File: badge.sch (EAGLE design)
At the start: 142 parts, among them CN4 MicroUSB, IC3 MEGA8-AI, T1 MMUN2133LT1G, U1 TPS61090RSAR, U2 MCP73871, Y1 16.00MHz

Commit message: Cut down the LEDs to 50 and added filter caps for each
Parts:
- removed +5V, GND, MISO, MOSI, RST, SCK: TPTP17R, testpad:TPTP17R
- removed LED100, LED51, LED52, LED53, LED54, LED55, LED56, LED57, LED58, LED59, LED60, LED61, LED62, LED63, LED64, LED65, LED66, LED67, LED68, LED69, LED70, LED71, LED72, LED73, LED74, LED75, LED76, LED77, LED78, LED79, LED80, LED81, LED82, LED83, LED84, LED85, LED86, LED87, LED88, LED89, LED90, LED91, LED92, LED93, LED94, LED95, LED96, LED97, LED98, LED99: WS2812B5050-NARROW, defcon:WS2812B5050-NARROW
- added C10, C11, C12, C13, C14, C15, C16, C17, C18, C19, C20, C21, C22, C23, C24, C25, C26, C27, C28, C29, C30, C31, C32, C33, C34, C35, C36, C37, C38, C39, C40, C41, C42, C43, C44, C45, C46, C47, C48, C49, C50, C51, C52, C53, C54, C55, C56, C57, C58, C9: (no value), resistor:C-USC0603
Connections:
- removed net HR_SET: JP1.1, MISO.TP
- removed net MIN_SET: JP1.3, SCK.TP
- new net MISO: IC3.PB4(MISO), JP1.1
- new net N$17: C9.1, LED1.VDD
- new net N$18: C9.2, LED1.GND
- new net SCK: IC3.PB5(SCK), JP1.3
- net +5V: no longer +5V.TP
- net GND: no longer GND.TP
- net MOSI: now also IC3.PB3(MOSI/OC2); no longer MOSI.TP
- net RESET_PROG: no longer RST.TP

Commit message: Added accelerometer circuitry
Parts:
- added C59: 0.1uF, resistor:C-USC0805
- added C60, C61: 10µF, resistor:C-USC0805
- added D2: 1N4148, led:LEDCHIP-LED0805
- added JP2: (no value), microbuilder:HEADER-1X870MIL
- added JP3: (no value), microbuilder:HEADER-1X3ROUND
- added Q1, Q2: BSS138, microbuilder:MOSFET-NWIDE
- added R10, R11, R12, R15, R18, R9: 10K, resistor:R-US_M0805
- added U3: LIS3DHTR, microbuilder:ACCEL_LIS3DHTR
- added U4: MIC5225-3.3, microbuilder:VREG_SOT23-5
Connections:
- new net 3.3V: C59.1, C60.1, JP2.2, Q1.G, Q2.G, R10.2, R11.2, R9.2, U3.VDD, U3.VDDIO, U4.OUT
- new net ADC1: JP3.1, U3.ADC1
- new net ADC2: JP3.2, U3.ADC2
- new net ADC3: JP3.3, U3.ADC3
- new net CS: D2.C, JP2.7
- new net INT1: JP2.8, U3.INT1
- new net N$19: D2.A, R9.1, U3.CS
- new net SCL: JP2.4, Q2.D, R15.1
- new net SCL_3.3V: Q2.S, R11.1, U3.SCL
- new net SDA: JP2.5, Q1.D, R12.1
- new net SDA_3.3V: Q1.S, R10.1, U3.SDA
- new net SDO: JP2.6, R18.2, U3.SDO
- new net VIN: C61.1, JP2.1, R12.2, R15.2, U4.EN, U4.IN
- net GND: now also C59.2, C60.2, C61.2, JP2.3, R18.1, U3.GND@1, U3.GND@2, U3.RES(GND), U4.GND
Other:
- note added: "* CS needs to be set off board to select SPI or I2C"
- note added: "Bus Selection"
- note added: "CS High = I2C, Low = SPI"
- note added: "Defaults to I2C as-is (R8)"
- note added: "I2C"
- note added: "LED Array"
- note added: "MCU Circuitry"
- note added: "Power Circuitry"
- note added: "SCL (Pin 4) = Serial Clock"
- note added: "SD0 (Pin 7) = SA0/Address LSB"
- note added: "SDA (Pin 6) = Data In (MOSI)"
- note added: "SDA (Pin 6) = Serial Data"
- note added: "SDO (Pin 7) = Data Out (MISO)"
- note added: "SDO pulled low by default (R1) to set I2C address LSB to 0"
- note added: "SPI"
- note added: "Set SJ1 to make I2C"
- note added: "address LSB 1"
- moved on the sheet: BT1, C1, C2, C4, C6, C7, C8, CHRG/LBO, CN4, DONE, JP1, L1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

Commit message: Added switches, status lights, RX/TX Headers
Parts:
- removed D2: 1N4148, led:LEDCHIP-LED0805
- removed JP3: (no value), microbuilder:HEADER-1X3ROUND
- added C62: 1F, resistor:CPOL-USE5-8.5
- added C63, C64, C65, C66, C67, C68: 100nF, resistor:C-USC0805
- added R19: 470, resistor:R-US_R0805
- added R21, R22, R23: 220, resistor:R-US_M0805
- added R24, R25, R26, R27, R28, R29: 1k, resistor:R-US_M0805
- added S1: (no value), adafruit:EG1218S
- added STAT1, STAT2, STAT3: GREEN, piboy_new:ADAFRUIT_LEDCHIPLED_0603
- added SV1: (no value), con-lstb:MA04-2
- added SW1, SW2, SW3, SW4, SW5, SW6: (no value), adafruit:SWITCH_PUSHBUTTONEVQ-PE
- JP1: device pinhead+:PINHD-2X3SMT -> pinhead:PINHD-2X4
- JP2: device microbuilder:HEADER-1X870MIL -> pinhead:PINHD-1X2
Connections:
- removed net CS: D2.C, JP2.7
- removed net ENABLE: R13.2, U1.EN
- new net BOOST_ENABLE: R13.2, S1.P, U1.EN
- new net CE\: SV1.6
- new net CSN: SV1.5
- new net N$20: R21.2, STAT2.C
- new net N$21: R22.2, STAT3.C
- new net N$22: R23.2, STAT1.C
- new net N$23: R24.2, SW1.P$2
- new net N$30: R26.2, SW3.P$2
- new net N$31: R28.2, SW5.P$2
- new net N$32: R29.2, SW6.P$2
- new net N$33: R27.2, SW4.P$2
- new net N$34: R25.2, SW2.P$2
- new net NEO-DOUT: IC3.PD6(AIN0), R19.1
- new net PIEZO: IC3.PB1(OC1A), JP2.1
- new net RX: IC3.PD0(RXD), JP1.7
- new net STAT1: IC3.PD2(INT0), STAT1.A
- new net STAT2: IC3.PD3(INT1)
- new net STAT3: IC3.PD4(XCK/T0), STAT3.A
- new net STAT4: STAT2.A
- new net SW1: C63.1, IC3.PC0(ADC0), R24.1
- new net SW2: C64.1, IC3.PC1(ADC1), R25.1
- new net SW3: C65.1, IC3.PC2(ADC2), R26.1
- new net SW4: C66.1, IC3.PC3(ADC3), R27.1
- new net SW5: C67.1, IC3.ADC6, R28.1
- new net SW6: C68.1, IC3.ADC7, R29.1
- new net TX: IC3.PD1(TXD), JP1.8
- net +5V: now also C62.+
- net 3.3V: now also R9.1, SV1.7; no longer JP2.2, R9.2
- net ADC1: no longer JP3.1
- net ADC2: no longer JP3.2
- net ADC3: no longer JP3.3
- net GND: now also C62.-, JP2.2, R21.1, R22.1, R23.1, S1.S, SV1.8, SW1.P$1, SW2.P$1, SW3.P$1, SW4.P$1, SW5.P$1, SW6.P$1; no longer JP2.3
- net INT1: no longer JP2.8
- net MISO: now also SV1.2
- net MOSI: now also SV1.3
- net N$19: now also R9.2; no longer D2.A, R9.1
- net SCK: now also SV1.4
- net SCL: now also IC3.PC5(ADC5/SCL); no longer JP2.4
- net SDA: now also IC3.PC4(ADC4/SDA); no longer JP2.5
- net SDO: no longer JP2.6
- net VIN: no longer JP2.1
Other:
- moved on the sheet: C59, C60, C61, Q1, Q2, R10, R11, R12, R15, R18, R9, U3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

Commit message: -wired all the pixels -cleaned up the schematic
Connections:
- removed net N$18: C9.2, LED1.GND
- new net N$24: LED1.DO, LED2.DI
- new net N$25: LED3.DO, LED4.DI
- new net N$26: LED4.DO, LED5.DI
- new net N$27: LED5.DO, LED6.DI
- new net N$37: LED6.DO, LED7.DI
- new net N$38: LED7.DO, LED8.DI
- new net N$39: LED8.DO, LED9.DI
- new net N$40: LED10.DI, LED9.DO
- new net N$41: LED10.DO, LED11.DI
- new net N$42: LED11.DO, LED12.DI
- new net N$43: LED12.DO, LED13.DI
- new net N$44: LED13.DO, LED14.DI
- new net N$45: LED14.DO, LED15.DI
- new net N$46: LED15.DO, LED16.DI
- new net N$47: LED16.DO, LED17.DI
- new net N$48: LED17.DO, LED18.DI
- new net N$49: LED18.DO, LED19.DI
- new net N$50: LED19.DO, LED20.DI
- new net N$51: LED20.DO, LED21.DI
- new net N$52: LED21.DO, LED22.DI
- new net N$53: LED22.DO, LED23.DI
- new net N$54: LED23.DO, LED24.DI
- new net N$55: LED24.DO, LED25.DI
- new net N$56: LED25.DO, LED26.DI
- new net N$57: LED26.DO, LED27.DI
- new net N$58: LED27.DO, LED28.DI
- new net N$59: LED28.DO, LED29.DI
- new net N$60: LED29.DO, LED30.DI
- new net N$61: LED30.DO, LED31.DI
- new net N$62: LED31.DO, LED32.DI
- new net N$63: LED32.DO, LED33.DI
- new net N$64: LED33.DO, LED34.DI
- new net N$65: LED34.DO, LED35.DI
- new net N$66: LED35.DO, LED36.DI
- new net N$67: LED36.DO, LED37.DI
- new net N$68: LED37.DO, LED38.DI
- new net N$69: LED38.DO, LED39.DI
- new net N$70: LED39.DO, LED40.DI
- new net N$71: LED40.DO, LED41.DI
- new net N$72: LED41.DO, LED42.DI
- new net N$73: LED42.DO, LED43.DI
- new net N$74: LED43.DO, LED44.DI
- new net N$75: LED44.DO, LED45.DI
- new net N$76: LED45.DO, LED46.DI
- new net N$77: LED46.DO, LED47.DI
- new net N$78: LED47.DO, LED48.DI
- new net N$79: LED48.DO, LED49.DI
- new net N$80: LED49.DO, LED50.DI
- new net PIXEL_DATA: LED1.DI, R19.2
- net +5V: now also C10.1, C11.1, C12.1, C13.1, C14.1, C15.1, C16.1, C17.1, C18.1, C19.1, C20.1, C21.1, C22.1, C23.1, C24.1, C25.1, C26.1, C27.1, C28.1, C29.1, C30.1, C31.1, C32.1, C33.1, C34.1, C35.1, C36.1, C37.1, C38.1, C39.1, C40.1, C41.1, C42.1, C43.1, C44.1, C45.1, C46.1, C47.1, C48.1, C49.1, C50.1, C51.1, C52.1, C53.1, C54.1, C55.1, C56.1, C57.1, C58.1, C9.1, LED1.VDD, LED10.VDD, LED11.VDD, LED12.VDD, LED13.VDD, LED14.VDD, LED15.VDD, LED16.VDD, LED17.VDD, LED18.VDD, LED19.VDD, LED2.VDD, LED20.VDD, LED21.VDD, LED22.VDD, LED23.VDD, LED24.VDD, LED25.VDD, LED26.VDD, LED27.VDD, LED28.VDD, LED29.VDD, LED3.VDD, LED30.VDD, LED31.VDD, LED32.VDD, LED33.VDD, LED34.VDD, LED35.VDD, LED36.VDD, LED37.VDD, LED38.VDD, LED39.VDD, LED4.VDD, LED40.VDD, LED41.VDD, LED42.VDD, LED43.VDD, LED44.VDD, LED45.VDD, LED46.VDD, LED47.VDD, LED48.VDD, LED49.VDD, LED5.VDD, LED50.VDD, LED6.VDD, LED7.VDD, LED8.VDD, LED9.VDD
- net GND: now also C10.2, C11.2, C12.2, C13.2, C14.2, C15.2, C16.2, C17.2, C18.2, C19.2, C20.2, C21.2, C22.2, C23.2, C24.2, C25.2, C26.2, C27.2, C28.2, C29.2, C30.2, C31.2, C32.2, C33.2, C34.2, C35.2, C36.2, C37.2, C38.2, C39.2, C40.2, C41.2, C42.2, C43.2, C44.2, C45.2, C46.2, C47.2, C48.2, C49.2, C50.2, C51.2, C52.2, C53.2, C54.2, C55.2, C56.2, C57.2, C58.2, C63.2, C64.2, C65.2, C66.2, C67.2, C68.2, C9.2, LED1.GND, LED10.GND, LED11.GND, LED12.GND, LED13.GND, LED14.GND, LED15.GND, LED16.GND, LED17.GND, LED18.GND, LED19.GND, LED2.GND, LED20.GND, LED21.GND, LED22.GND, LED23.GND, LED24.GND, LED25.GND, LED26.GND, LED27.GND, LED28.GND, LED29.GND, LED3.GND, LED30.GND, LED31.GND, LED32.GND, LED33.GND, LED34.GND, LED35.GND, LED36.GND, LED37.GND, LED38.GND, LED39.GND, LED4.GND, LED40.GND, LED41.GND, LED42.GND, LED43.GND, LED44.GND, LED45.GND, LED46.GND, LED47.GND, LED48.GND, LED49.GND, LED5.GND, LED50.GND, LED6.GND, LED7.GND, LED8.GND, LED9.GND
- net N$17: now also LED2.DO, LED3.DI; no longer C9.1, LED1.VDD
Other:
- moved on the sheet: C65, C66, C67, C68, R26, R27, R28, R29, SW3, SW4, SW5, SW6

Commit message: haha forget to save fuck me
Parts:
- removed SV1: (no value), con-lstb:MA04-2
- added JP3: TCVR_HEADER, pinhead:PINHD-2X4
- JP2: value (none) -> PIEZO_HEADER
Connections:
- removed net ADC1: U3.ADC1
- removed net ADC2: U3.ADC2
- removed net ADC3: U3.ADC3
- removed net INT1: U3.INT1
- removed net STAT4: STAT2.A
- net 3.3V: now also JP3.7; no longer SV1.7
- net CE\: now also JP3.6; no longer SV1.6
- net CSN: now also JP3.5; no longer SV1.5
- net GND: now also JP3.8; no longer SV1.8
- net MISO: now also JP3.2; no longer SV1.2
- net MOSI: now also JP3.3; no longer SV1.3
- net SCK: now also JP3.4; no longer SV1.4
- net STAT2: now also STAT2.A
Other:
- note added: "Headers"
- moved on the sheet: BT1, C7, C8, CHRG/LBO, CN4, DONE, JP1, JP2, R14, R16, R17, R21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

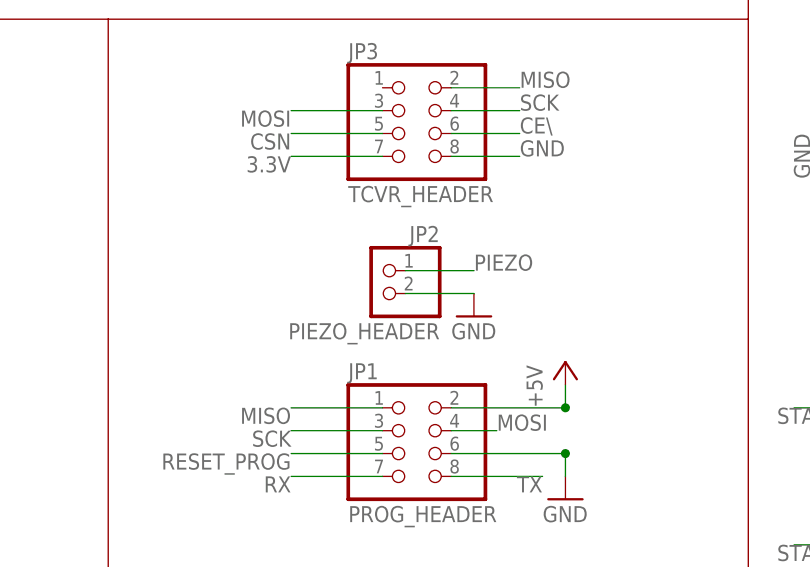
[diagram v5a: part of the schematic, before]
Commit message: small silkscreen changes
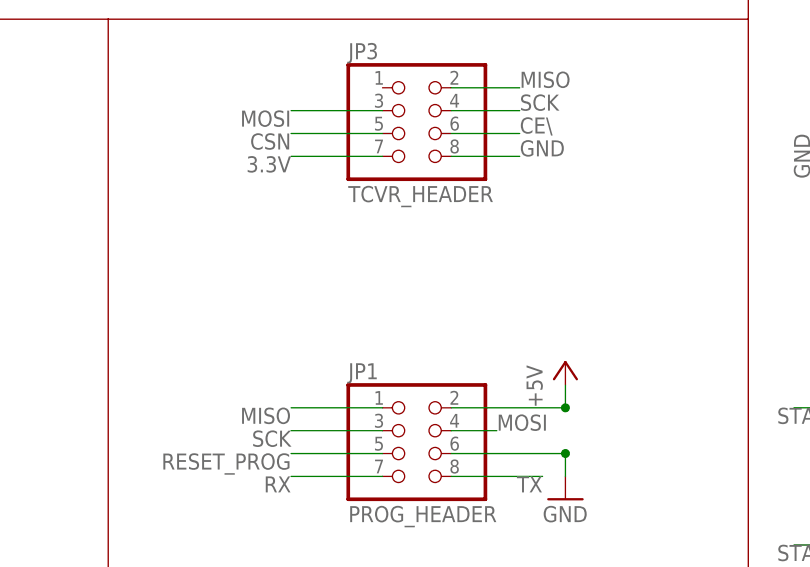
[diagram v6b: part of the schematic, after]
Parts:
- removed JP2: PIEZO_HEADER, pinhead:PINHD-1X2
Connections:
- net GND: no longer JP2.2
- net PIEZO: no longer JP2.1
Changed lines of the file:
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@@
 <part name="C62" library="resistor" library_urn="urn:adsk.eagle:library:348" deviceset="CPOL-US" device="E5-8.5" package3d_urn="urn:adsk.eagle:package:25860/1" value="1F"/>
 <part name="U$21" library="microbuilder" deviceset="GND" device=""/>
-<part name="JP2" library="pinhead" library_urn="urn:adsk.eagle:library:325" deviceset="PINHD-1X2" device="" package3d_urn="urn:adsk.eagle:package:22435/2" value="PIEZO_HEADER"/>
-<part name="GND8" library="supply1" library_urn="urn:adsk.eagle:library:371" deviceset="GND" device=""/>
 <part name="GND12" library="supply1" library_urn="urn:adsk.eagle:library:371" deviceset="GND" device=""/>
 <part name="GND13" library="supply1" library_urn="urn:adsk.eagle:library:371" deviceset="GND" device=""/>
@@
 <instance part="C62" gate="G$1" x="-48.26" y="-2.54"/>
 <instance part="U$21" gate="G$1" x="-48.26" y="-12.7"/>
-<instance part="JP2" gate="G$1" x="-314.96" y="-109.22" rot="MR0"/>
-<instance part="GND8" gate="1" x="-304.8" y="-111.76"/>
 <instance part="GND12" gate="1" x="-266.7" y="-50.8" rot="R270"/>
 <instance part="GND13" gate="1" x="-220.98" y="-50.8" rot="R270"/>
@@
 <pinref part="U$21" gate="G$1" pin="GND"/>
 <wire x1="-48.26" y1="-10.16" x2="-48.26" y2="-7.62" width="0.1524" layer="91"/>
-</segment>
-<segment>
-<pinref part="JP2" gate="G$1" pin="2"/>
-<wire x1="-312.42" y1="-109.22" x2="-304.8" y2="-109.22" width="0.1524" layer="91"/>
-<pinref part="GND8" gate="1" pin="GND"/>
 </segment>
 <segment>
@@
 <net name="PIEZO" class="0">
 <segment>
-<pinref part="JP2" gate="G$1" pin="1"/>
-<wire x1="-312.42" y1="-106.68" x2="-304.8" y2="-106.68" width="0.1524" layer="91"/>
-<label x="-304.8" y="-106.68" size="1.778" layer="95"/>
-</segment>
-<segment>
 <pinref part="IC3" gate="G$1" pin="PB1(OC1A)"/>

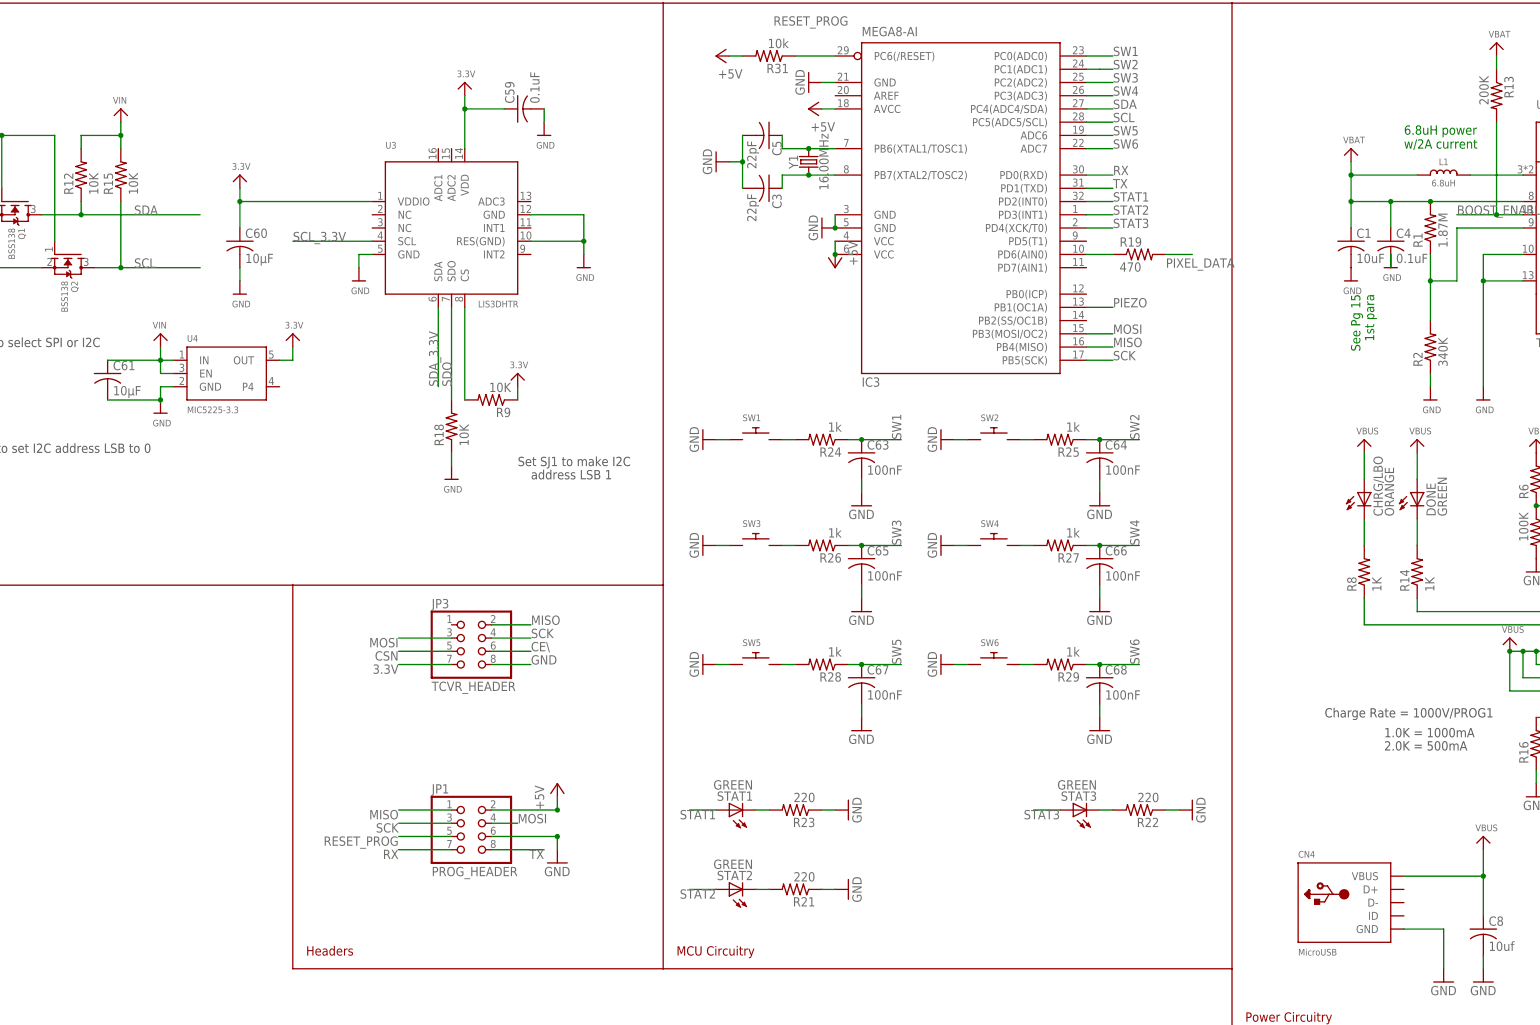
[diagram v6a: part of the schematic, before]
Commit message: Routed all the traces and performed a cursory DRC
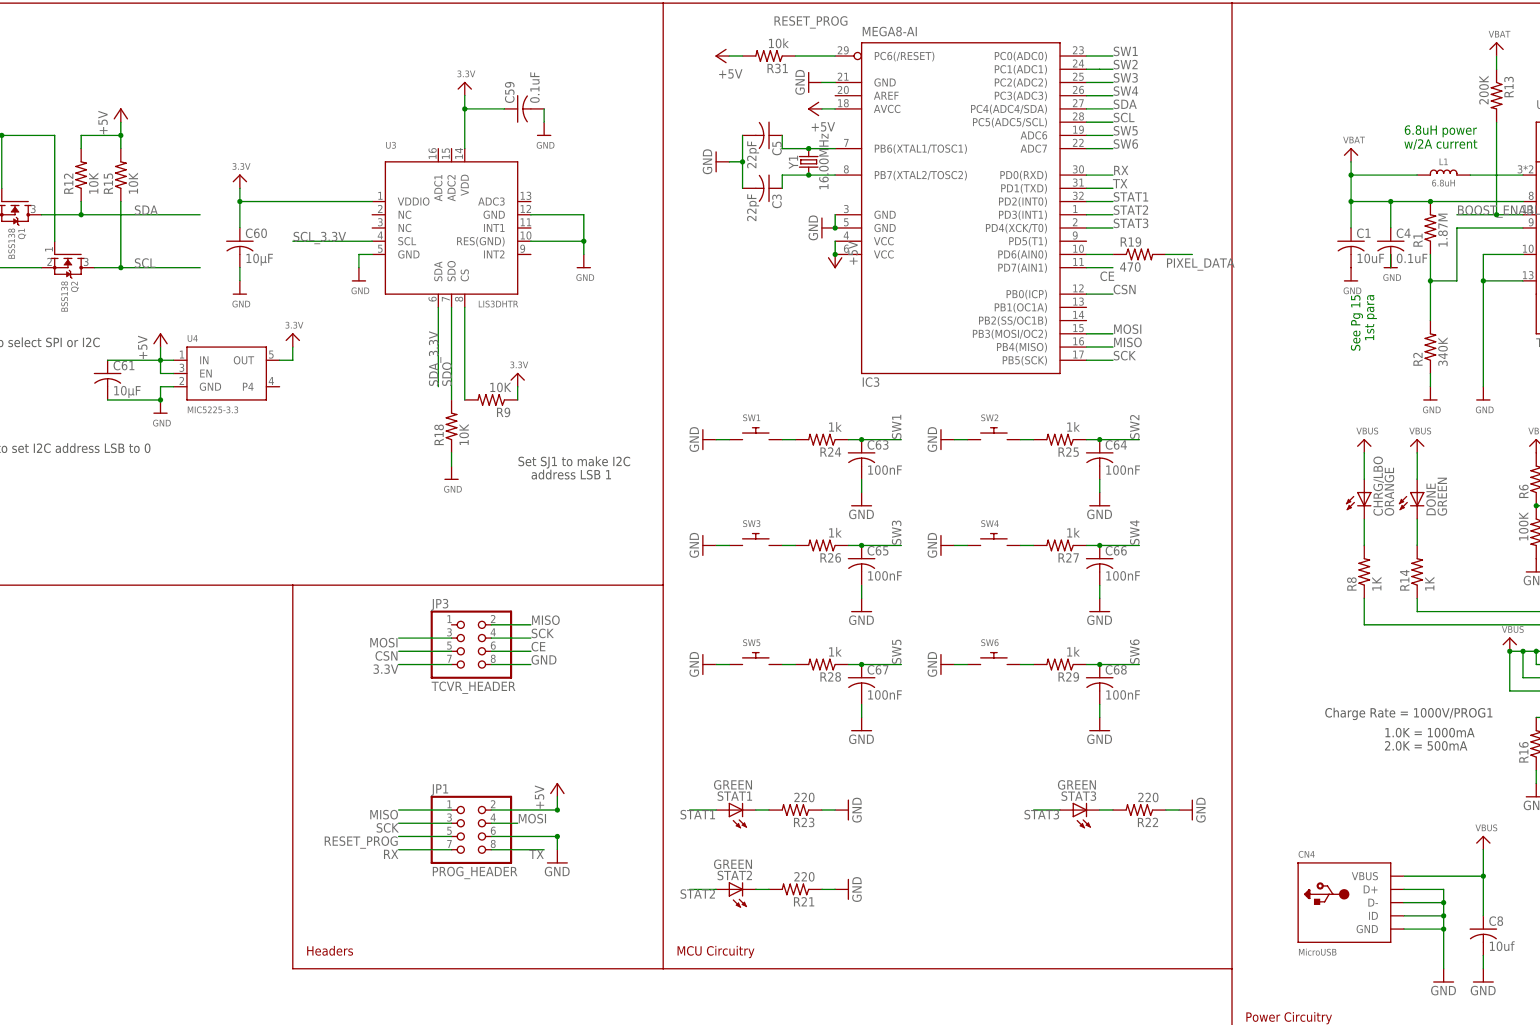
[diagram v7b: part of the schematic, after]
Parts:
- C3, C5, C59, C63, C64, C65, C66, C67, C68: device resistor:C-USC0805 -> resistor:C-USC0603
- R10, R11, R12, R15, R18, R24, R25, R26, R27, R28, R29, R9: device resistor:R-US_M0805 -> resistor:R-US_R0603
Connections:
- removed net CE\: JP3.6
- removed net PIEZO: IC3.PB1(OC1A)
- removed net VIN: C61.1, R12.2, R15.2, U4.EN, U4.IN
- new net CE: IC3.PD7(AIN1), JP3.6
- net +5V: now also C61.1, R12.2, R15.2, U4.EN, U4.IN
- net CSN: now also IC3.PB0(ICP)
- net GND: now also CN4.D+, CN4.D-, CN4.ID
